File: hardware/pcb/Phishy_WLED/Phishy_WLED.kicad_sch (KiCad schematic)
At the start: 17 parts, among them J3 Screw_Terminal_01x05, J4 Screw_Terminal_01x04, J5 Screw_Terminal_01x04, J6 Conn_01x06, SW1 SW_Push, SW2 SW_Push, SW3 SW_Push, U2 ESP32-WROOM-32D

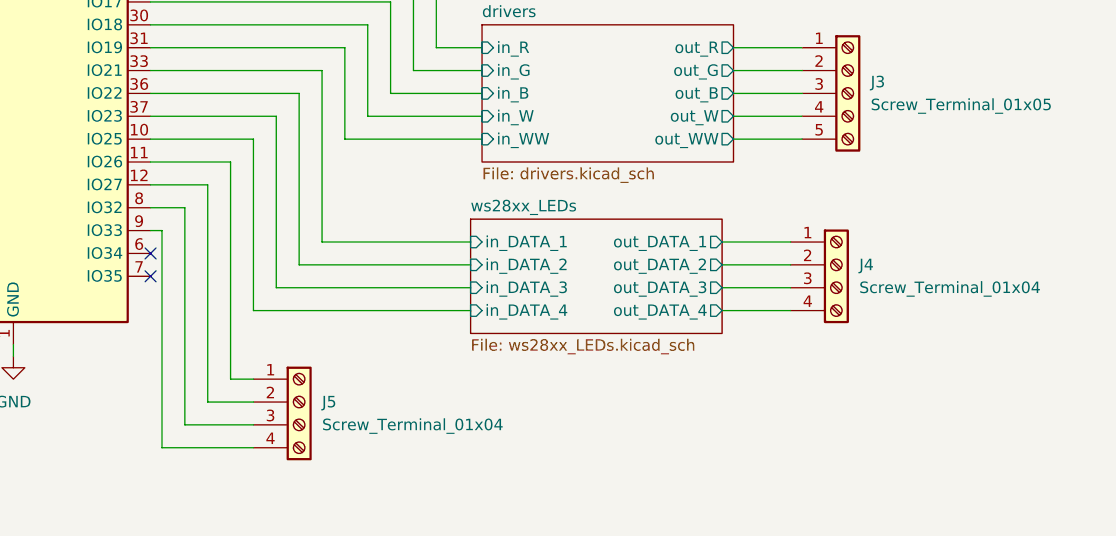
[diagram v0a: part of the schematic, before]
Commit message: footprints added !
all the footprints are here
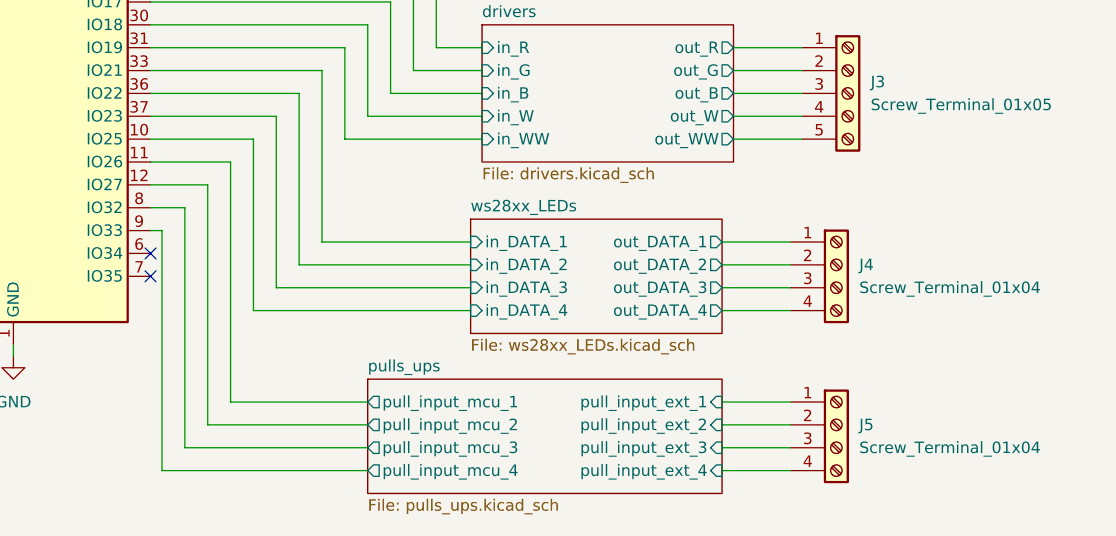
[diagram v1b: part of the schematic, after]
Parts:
- D2: footprint (none) -> LED_SMD:LED_0603_1608Metric
- J3: footprint (none) -> TerminalBlock_TE-Connectivity:TerminalBlock_TE_282834-5_1x05_P2.54mm_Horizontal
- J4, J5: footprint (none) -> Connector_PinSocket_2.54mm:PinSocket_1x04_P2.54mm_Vertical
- J6: footprint (none) -> Connector_PinSocket_2.54mm:PinSocket_1x06_P2.54mm_Vertical
- R3: footprint (none) -> Resistor_SMD:R_0603_1608Metric
- SW1, SW2, SW3: footprint (none) -> Button_Switch_THT:SW_PUSH_6mm_H5mm
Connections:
- net pulls_ups/pull_input_ext_1: now reaches J5.1 (Pin_1)
- net pulls_ups/pull_input_ext_1: no longer U2.11 (IO26)
- net pulls_ups/pull_input_ext_2: now reaches J5.2 (Pin_2)
- net pulls_ups/pull_input_ext_2: no longer U2.12 (IO27)
- net pulls_ups/pull_input_ext_3: now reaches J5.3 (Pin_3)
- net pulls_ups/pull_input_ext_3: no longer U2.8 (IO32)
- net pulls_ups/pull_input_ext_4: now reaches J5.4 (Pin_4)
- net pulls_ups/pull_input_ext_4: no longer U2.9 (IO33)
- new net pulls_ups/pull_input_mcu_1: U2.11 (IO26)
- new net pulls_ups/pull_input_mcu_2: U2.12 (IO27)
- new net pulls_ups/pull_input_mcu_3: U2.8 (IO32)
- new net pulls_ups/pull_input_mcu_4: U2.9 (IO33)
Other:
- added sheet pulls_ups (pulls_ups.kicad_sch)
- moved on the sheet: J5
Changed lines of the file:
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@@
     (stroke (width 0) (type default))
   )
-  (wire (pts (xy 128.27 137.16) (xy 135.89 137.16))
+  (wire (pts (xy 128.27 139.7) (xy 148.59 139.7))
     (stroke (width 0) (type default))
   )
@@
     (stroke (width 0) (type default))
   )
+  (wire (pts (xy 187.96 139.7) (xy 195.58 139.7))
+    (stroke (width 0) (type default))
+  )
   (wire (pts (xy 153.67 87.63) (xy 153.67 97.79))
     (stroke (width 0) (type default))
@@
     (stroke (width 0) (type default))
   )
-  (wire (pts (xy 125.73 115.57) (xy 125.73 139.7))
+  (wire (pts (xy 125.73 115.57) (xy 125.73 142.24))
     (stroke (width 0) (type default))
   )
@@
     (stroke (width 0) (type default))
   )
-  (wire (pts (xy 130.81 134.62) (xy 135.89 134.62))
+  (wire (pts (xy 130.81 137.16) (xy 148.59 137.16))
     (stroke (width 0) (type default))
   )
@@
     (stroke (width 0) (type default))
   )
-  (wire (pts (xy 128.27 113.03) (xy 128.27 137.16))
+  (wire (pts (xy 187.96 137.16) (xy 195.58 137.16))
+    (stroke (width 0) (type default))
+  )
+  (wire (pts (xy 187.96 142.24) (xy 195.58 142.24))
+    (stroke (width 0) (type default))
+  )
+  (wire (pts (xy 128.27 113.03) (xy 128.27 139.7))
     (stroke (width 0) (type default))
   )
@@
     (stroke (width 0) (type default))
   )
-  (wire (pts (xy 135.89 132.08) (xy 133.35 132.08))
+  (wire (pts (xy 133.35 134.62) (xy 148.59 134.62))
     (stroke (width 0) (type default))
   )
@@
     (stroke (width 0) (type default))
   )
-  (wire (pts (xy 133.35 132.08) (xy 133.35 107.95))
+  (wire (pts (xy 133.35 134.62) (xy 133.35 107.95))
     (stroke (width 0) (type default))
   )
@@
     (stroke (width 0) (type default))
   )
-  (wire (pts (xy 130.81 110.49) (xy 130.81 134.62))
+  (wire (pts (xy 130.81 110.49) (xy 130.81 137.16))
     (stroke (width 0) (type default))
   )
@@
     (stroke (width 0) (type default))
   )
+  (wire (pts (xy 187.96 134.62) (xy 195.58 134.62))
+    (stroke (width 0) (type default))
+  )
   (wire (pts (xy 138.43 121.92) (xy 138.43 102.87))
     (stroke (width 0) (type default))
@@
     (stroke (width 0) (type default))
   )
-  (wire (pts (xy 125.73 139.7) (xy 135.89 139.7))
+  (wire (pts (xy 125.73 142.24) (xy 148.59 142.24))
     (stroke (width 0) (type default))
   )
@@
       (effects (font (size 1.27 1.27)) (justify right))
     )
-    (property "Footprint" "" (at 74.168 53.34 90)
+    (property "Footprint" "Resistor_SMD:R_0603_1608Metric" (at 74.168 53.34 90)
       (effects (font (size 1.27 1.27)) hide)
     )
@@
       (effects (font (size 1.27 1.27)))
     )
-    (property "Footprint" "" (at 146.05 57.15 0)
+    (property "Footprint" "Button_Switch_THT:SW_PUSH_6mm_H5mm" (at 146.05 57.15 0)
       (effects (font (size 1.27 1.27)) hide)
     )
@@
       (effects (font (size 1.27 1.27)) (justify right))
     )
-    (property "Footprint" "" (at 187.198 57.15 90)
+    (property "Footprint" "Resistor_SMD:R_0603_1608Metric" (at 187.198 57.15 90)
       (effects (font (size 1.27 1.27)) hide)
     )
@@
       (effects (font (size 1.27 1.27)) (justify right))
     )
-    (property "Footprint" "" (at 136.398 52.07 90)
+    (property "Footprint" "Resistor_SMD:R_0603_1608Metric" (at 136.398 52.07 90)
       (effects (font (size 1.27 1.27)) hide)
     )
@@
       (effects (font (size 1.27 1.27)))
     )
-    (property "Footprint" "" (at 54.61 57.15 0)
+    (property "Footprint" "Button_Switch_THT:SW_PUSH_6mm_H5mm" (at 54.61 57.15 0)
       (effects (font (size 1.27 1.27)) hide)
     )
@@
       (effects (font (size 1.27 1.27)))
     )
-    (property "Footprint" "" (at 193.04 67.31 0)
+    (property "Footprint" "Button_Switch_THT:SW_PUSH_6mm_H5mm" (at 193.04 67.31 0)
       (effects (font (size 1.27 1.27)) hide)
     )
@@
     )
   )
-  (symbol (lib_id "Connector:Screw_Terminal_01x04") (at 140.97 134.62 0) (unit 1)
-    (in_bom yes) (on_board yes) (dnp no) (fields_autoplaced)
-    (property "Reference" "J5" (at 143.51 134.62 0)
-      (effects (font (size 1.27 1.27)) (justify left))
-    )
-    (property "Value" "Screw_Terminal_01x04" (at 143.51 137.16 0)
-      (effects (font (size 1.27 1.27)) (justify left))
-    )
-    (property "Footprint" "" (at 140.97 134.62 0)
-      (effects (font (size 1.27 1.27)) hide)
-    )
-    (property "Datasheet" "~" (at 140.97 134.62 0)
+  (symbol (lib_id "Connector:Screw_Terminal_01x04") (at 200.66 137.16 0) (unit 1)
+    (in_bom yes) (on_board yes) (dnp no) (fields_autoplaced)
+    (property "Reference" "J5" (at 203.2 137.16 0)
+      (effects (font (size 1.27 1.27)) (justify left))
+    )
+    (property "Value" "Screw_Terminal_01x04" (at 203.2 139.7 0)
+      (effects (font (size 1.27 1.27)) (justify left))
+    )
+    (property "Footprint" "Connector_PinSocket_2.54mm:PinSocket_1x04_P2.54mm_Vertical" (at 200.66 137.16 0)
+      (effects (font (size 1.27 1.27)) hide)
+    )
+    (property "Datasheet" "~" (at 200.66 137.16 0)
       (effects (font (size 1.27 1.27)) hide)
     )
@@
       (effects (font (size 1.27 1.27)))
     )
-    (property "Footprint" "" (at 139.7 69.088 90)
+    (property "Footprint" "Resistor_SMD:R_0603_1608Metric" (at 139.7 69.088 90)
       (effects (font (size 1.27 1.27)) hide)
     )
@@
       (effects (font (size 1.27 1.27)))
     )
-    (property "Footprint" "" (at 151.13 67.31 0)
+    (property "Footprint" "LED_SMD:LED_0603_1608Metric" (at 151.13 67.31 0)
       (effects (font (size 1.27 1.27)) hide)
     )
@@
       (effects (font (size 1.27 1.27)) (justify left))
     )
-    (property "Footprint" "" (at 200.66 119.38 0)
+    (property "Footprint" "Connector_PinSocket_2.54mm:PinSocket_1x04_P2.54mm_Vertical" (at 200.66 119.38 0)
       (effects (font (size 1.27 1.27)) hide)
     )
@@
       (effects (font (size 1.27 1.27)))
     )
-    (property "Footprint" "" (at 167.64 39.37 0)
+    (property "Footprint" "Connector_PinSocket_2.54mm:PinSocket_1x06_P2.54mm_Vertical" (at 167.64 39.37 0)
       (effects (font (size 1.27 1.27)) hide)
     )
@@
       (effects (font (size 1.27 1.27)) (justify left))
     )
-    (property "Footprint" "" (at 201.93 100.33 0)
+    (property "Footprint" "TerminalBlock_TE-Connectivity:TerminalBlock_TE_282834-5_1x05_P2.54mm_Horizontal" (at 201.93 100.33 0)
       (effects (font (size 1.27 1.27)) hide)
     )
@@
       )
     )
+  )
+  (sheet (at 148.59 132.08) (size 39.37 12.7) (fields_autoplaced)
+    (stroke (width 0.1524) (type solid))
+    (fill (color 0 0 0 0.0000))
+    (property "Sheetname" "pulls_ups" (at 148.59 131.3684 0)
+      (effects (font (size 1.27 1.27)) (justify left bottom))
+    )
+    (property "Sheetfile" "pulls_ups.kicad_sch" (at 148.59 145.3646 0)
+      (effects (font (size 1.27 1.27)) (justify left top))
+    )
+    (pin "pull_input_mcu_3" output (at 148.59 139.7 180)
+      (effects (font (size 1.27 1.27)) (justify left))
+    )
+    (pin "pull_input_ext_1" input (at 187.96 134.62 0)
+      (effects (font (size 1.27 1.27)) (justify right))
+    )
+    (pin "pull_input_ext_3" input (at 187.96 139.7 0)
+      (effects (font (size 1.27 1.27)) (justify right))
+    )
+    (pin "pull_input_mcu_4" output (at 148.59 142.24 180)
+      (effects (font (size 1.27 1.27)) (justify left))
+    )
+    (pin "pull_input_ext_4" input (at 187.96 142.24 0)
+      (effects (font (size 1.27 1.27)) (justify right))
+    )
+    (pin "pull_input_mcu_2" output (at 148.59 137.16 180)
+      (effects (font (size 1.27 1.27)) (justify left))
+    )
+    (pin "pull_input_ext_2" input (at 187.96 137.16 0)
+      (effects (font (size 1.27 1.27)) (justify right))
+    )
+    (pin "pull_input_mcu_1" output (at 148.59 134.62 180)
+      (effects (font (size 1.27 1.27)) (justify left))
+    )
+    (instances
+      (project "Phishy_WLED"
+        (path "/04065f65-9c82-4e78-8d42-4173227f9ac1" (page "5"))
+      )
+    )
